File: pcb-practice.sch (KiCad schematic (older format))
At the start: 24 parts, among them SW1 SW_Push, U1 ATmega32U4-AU, Y1 16MHz

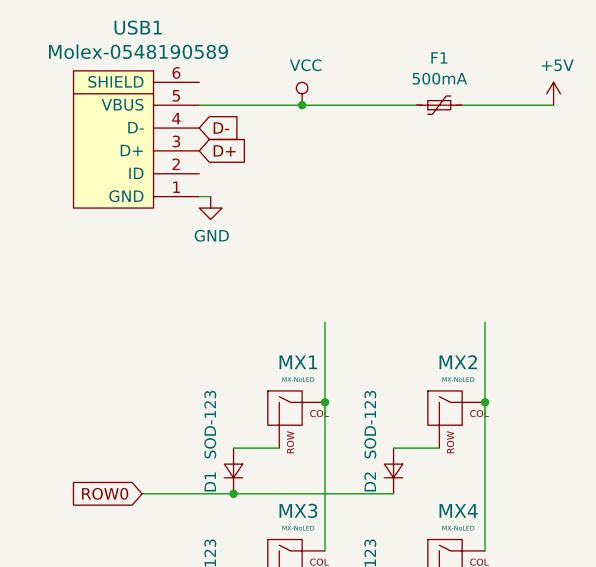
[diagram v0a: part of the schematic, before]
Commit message: placed components on pcb
pcb component layout up to routing
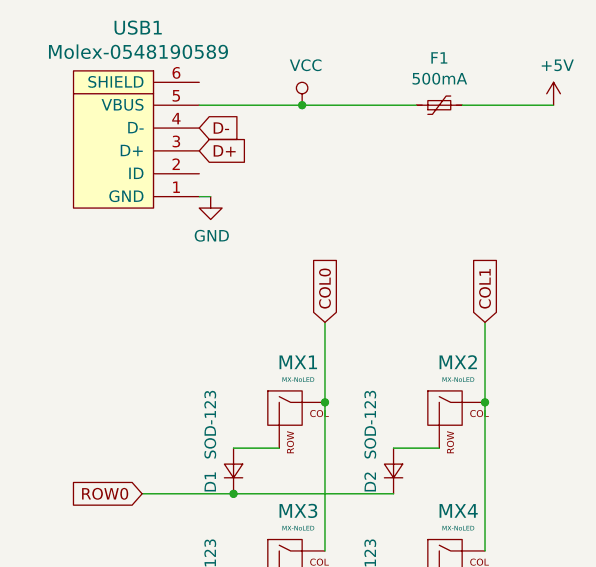
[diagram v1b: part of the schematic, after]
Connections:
- net labels added: COL0, COL1
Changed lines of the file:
@@
 Text GLabel 8200 5300 0    50   Input ~ 0
 ROW1
+Text GLabel 9000 3900 1    50   Input ~ 0
+COL0
+Text GLabel 9700 3900 1    50   Input ~ 0
+COL1
 $EndSCHEMATC
